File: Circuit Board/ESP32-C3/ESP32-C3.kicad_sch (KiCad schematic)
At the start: 19 parts

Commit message: Exposed General Purpose SPI & LED
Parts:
- added R?: 22R, symbol Device:R
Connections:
- net INT_ACC: now reaches U?.10 (MTDI/GPIO5/ADC2_CH0)
- net FSPI_CLK: now reaches U?.12 (MTCK/GPIO6)
- net FSPI_CLK: now also R?.2
- net FSPI_D: now reaches U?.13 (MTDO/GPIO7)
- net LED B: now reaches U?.9 (MTMS/GPIO4/ADC1_CH4)
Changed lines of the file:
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@@
     (stroke (width 0) (type default) (color 0 0 0 0))
   )
-  (wire (pts (xy 106.553 93.98) (xy 114.935 93.98))
+  (wire (pts (xy 94.996 93.98) (xy 114.935 93.98))
     (stroke (width 0) (type default) (color 0 0 0 0))
   )
@@
     (stroke (width 0) (type default) (color 0 0 0 0))
   )
+  (wire (pts (xy 104.648 99.06) (xy 114.935 99.06))
+    (stroke (width 0) (type default) (color 0 0 0 0))
+  )
   (wire (pts (xy 192.786 114.935) (xy 190.754 114.935))
     (stroke (width 0) (type default) (color 0 0 0 0))
@@
     (stroke (width 0) (type default) (color 0 0 0 0))
   )
-  (wire (pts (xy 106.553 96.52) (xy 114.935 96.52))
+  (wire (pts (xy 94.996 96.52) (xy 114.935 96.52))
     (stroke (width 0) (type default) (color 0 0 0 0))
   )
@@
     (stroke (width 0) (type default) (color 0 0 0 0))
   )
-  (wire (pts (xy 106.68 101.6) (xy 114.935 101.6))
+  (wire (pts (xy 94.996 101.6) (xy 114.935 101.6))
     (stroke (width 0) (type default) (color 0 0 0 0))
   )
@@
     (stroke (width 0) (type default) (color 0 0 0 0))
   )
-  (wire (pts (xy 106.553 99.06) (xy 114.935 99.06))
+  (wire (pts (xy 94.996 99.06) (xy 97.028 99.06))
     (stroke (width 0) (type default) (color 0 0 0 0))
   )
@@
   (text "CL=2*(CLO-Cs)=2*(10-5)pF=10pF" (at 72.136 53.594 0)
     (effects (font (size 1 1)) (justify left bottom))
+  )
+  (label "LED B" (at 106.299 93.98 0)
+    (effects (font (size 1.27 1.27)) (justify left bottom))
+  )
+  (label "FSPI_D" (at 105.029 101.6 0)
+    (effects (font (size 1.27 1.27)) (justify left bottom))
+  )
+  (label "FSPI_CLK" (at 105.029 99.06 0)
+    (effects (font (size 1.27 1.27)) (justify left bottom))
+  )
+  (label "INT_ACC" (at 105.41 96.52 0)
+    (effects (font (size 1.27 1.27)) (justify left bottom))
   )
   (global_label "SPI_NCS" (shape input) (at 171.958 96.52 0) (fields_autoplaced)
@@
     (pin "2")
   )
+  (symbol (lib_id "Device:R") (at 100.838 99.06 90) (unit 1)
+    (in_bom yes) (on_board yes)
+    (property "Reference" "R?" (id 0) (at 97.028 97.536 90))
+    (property "Value" "22R" (id 1) (at 100.711 99.187 90))
+    (property "Footprint" "" (id 2) (at 100.838 100.838 90)
+      (effects (font (size 1.27 1.27)) hide)
+    )
+    (property "Datasheet" "~" (id 3) (at 100.838 99.06 0)
+      (effects (font (size 1.27 1.27)) hide)
+    )
+    (pin "1")
+    (pin "2")
+  )
   (symbol (lib_id "Device:C") (at 118.364 56.642 0) (unit 1)
     (in_bom yes) (on_board yes) (fields_autoplaced)
@@
       (reference "R?") (unit 1) (value "22R") (footprint "")
     )
+    (path "/87b79b9a-bd1e-435d-9300-858b5850ef25"
+      (reference "R?") (unit 1) (value "22R") (footprint "")
+    )

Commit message: Added UART Pinout
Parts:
- added R? (x2): 470R, symbol Device:R
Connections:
- net at U?.27 (U0RXD/GPIO20): now also R?.1
- net at U?.28 (U0TXD/GPIO21): now also R?.1
- new net UART0_RX: R?.2
- new net UART0_TX: R?.2
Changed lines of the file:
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@@
+    (stroke (width 0) (type default) (color 0 0 0 0))
+  )
+  (wire (pts (xy 186.309 73.66) (xy 191.77 73.66))
     (stroke (width 0) (type default) (color 0 0 0 0))
   )
@@
     (stroke (width 0) (type default) (color 0 0 0 0))
   )
+  (wire (pts (xy 186.309 71.12) (xy 191.77 71.12))
+    (stroke (width 0) (type default) (color 0 0 0 0))
+  )
   (wire (pts (xy 112.268 51.054) (xy 118.364 51.054))
     (stroke (width 0) (type default) (color 0 0 0 0))
@@
     (stroke (width 0) (type default) (color 0 0 0 0))
   )
+  (wire (pts (xy 170.815 71.12) (xy 178.689 71.12))
+    (stroke (width 0) (type default) (color 0 0 0 0))
+  )
   (wire (pts (xy 78.105 124.46) (xy 66.675 124.46))
     (stroke (width 0) (type default) (color 0 0 0 0))
@@
   )
   (wire (pts (xy 175.895 124.46) (xy 175.895 128.27))
+    (stroke (width 0) (type default) (color 0 0 0 0))
+  )
+  (wire (pts (xy 170.815 73.66) (xy 178.689 73.66))
     (stroke (width 0) (type default) (color 0 0 0 0))
   )
@@
     (effects (font (size 1.27 1.27)) (justify left bottom))
   )
+  (label "UART0_RX" (at 187.071 73.66 0)
+    (effects (font (size 1.27 1.27)) (justify left bottom))
+  )
   (label "FSPI_D" (at 105.029 101.6 0)
     (effects (font (size 1.27 1.27)) (justify left bottom))
@@
   )
   (label "INT_ACC" (at 105.41 96.52 0)
+    (effects (font (size 1.27 1.27)) (justify left bottom))
+  )
+  (label "UART0_TX" (at 187.198 71.12 0)
     (effects (font (size 1.27 1.27)) (justify left bottom))
   )
@@
     (pin "2")
   )
+  (symbol (lib_id "Device:R") (at 182.499 73.66 90) (unit 1)
+    (in_bom yes) (on_board yes)
+    (property "Reference" "R?" (id 0) (at 182.499 75.692 90))
+    (property "Value" "470R" (id 1) (at 182.499 73.787 90))
+    (property "Footprint" "" (id 2) (at 182.499 75.438 90)
+      (effects (font (size 1.27 1.27)) hide)
+    )
+    (property "Datasheet" "~" (id 3) (at 182.499 73.66 0)
+      (effects (font (size 1.27 1.27)) hide)
+    )
+    (pin "1")
+    (pin "2")
+  )
   (symbol (lib_id "power:GND") (at 121.92 147.955 0) (unit 1)
     (in_bom yes) (on_board yes) (fields_autoplaced)
@@
     )
     (property "Datasheet" "~" (id 3) (at 131.445 135.89 0)
+      (effects (font (size 1.27 1.27)) hide)
+    )
+    (pin "1")
+    (pin "2")
+  )
+  (symbol (lib_id "Device:R") (at 182.499 71.12 90) (unit 1)
+    (in_bom yes) (on_board yes)
+    (property "Reference" "R?" (id 0) (at 182.499 69.215 90))
+    (property "Value" "470R" (id 1) (at 182.499 71.247 90))
+    (property "Footprint" "" (id 2) (at 182.499 72.898 90)
+      (effects (font (size 1.27 1.27)) hide)
+    )
+    (property "Datasheet" "~" (id 3) (at 182.499 71.12 0)
       (effects (font (size 1.27 1.27)) hide)
     )
@@
       (reference "R?") (unit 1) (value "22R") (footprint "")
     )
+    (path "/4c20fbfb-2772-4ac7-943c-c67b70ee00e3"
+      (reference "R?") (unit 1) (value "470R") (footprint "")
+    )
     (path "/87b79b9a-bd1e-435d-9300-858b5850ef25"
       (reference "R?") (unit 1) (value "22R") (footprint "")
@@
       (reference "R?") (unit 1) (value "5k1") (footprint "")
     )
+    (path "/d053cebc-ddcc-4fe9-8757-cc44e8daedcd"
+      (reference "R?") (unit 1) (value "470R") (footprint "")
+    )
     (path "/fe4df71a-c9dd-4482-86ce-3213aba20d79"

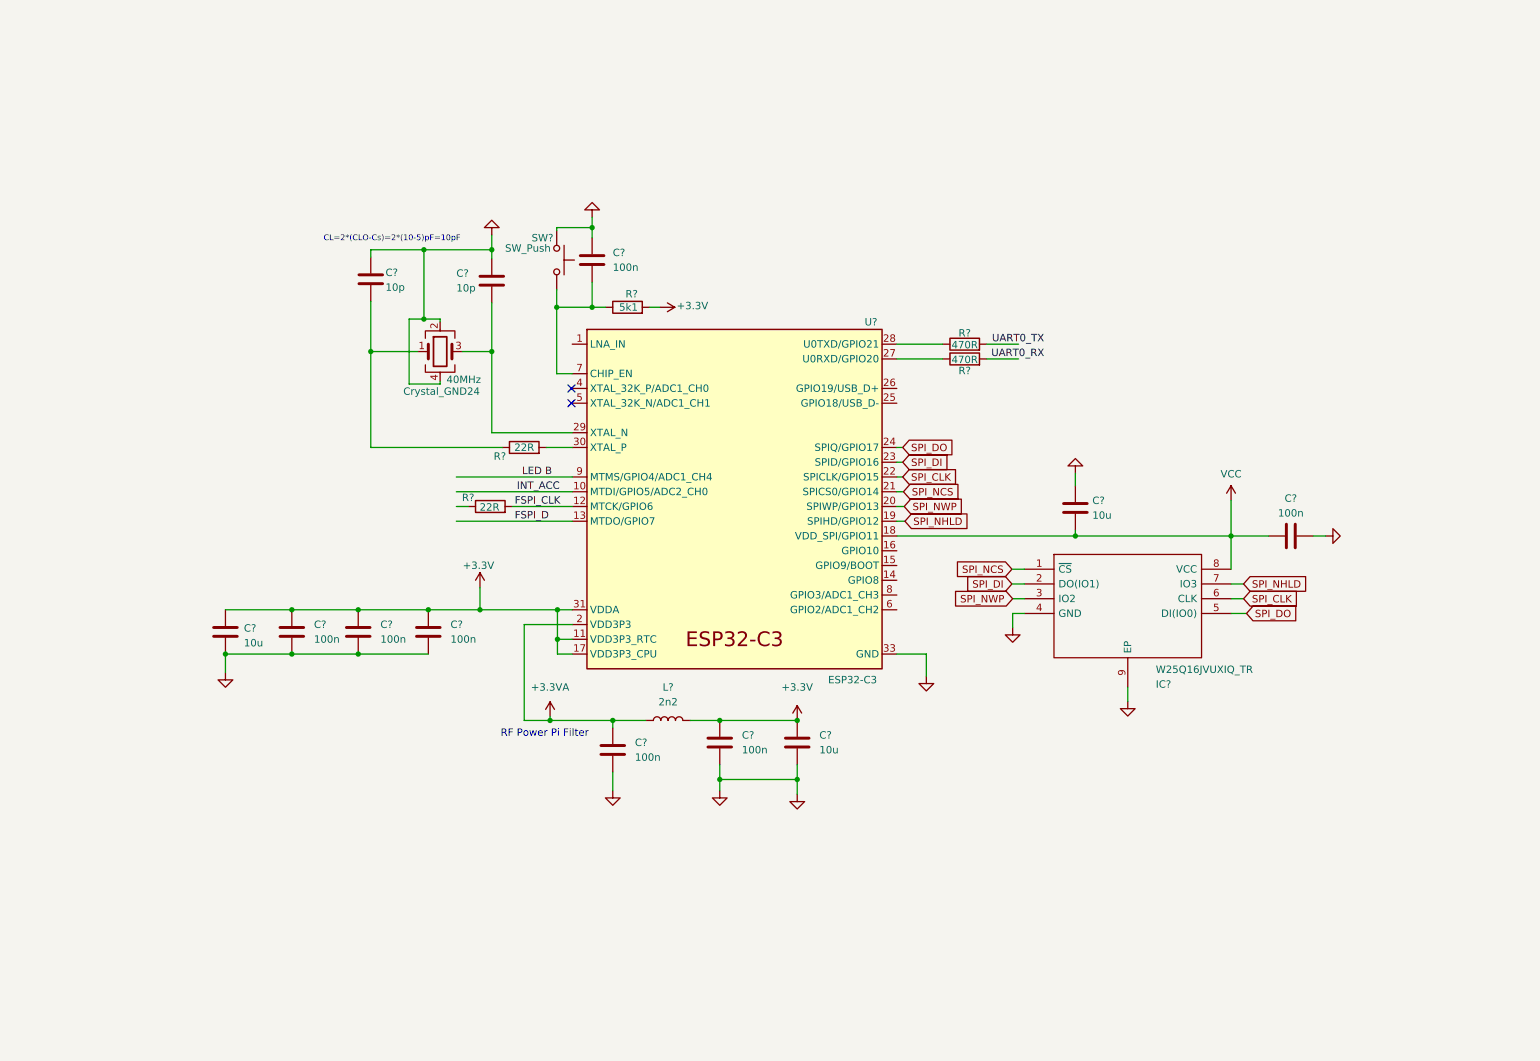
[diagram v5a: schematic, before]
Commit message: Added power regulator for USB C connector
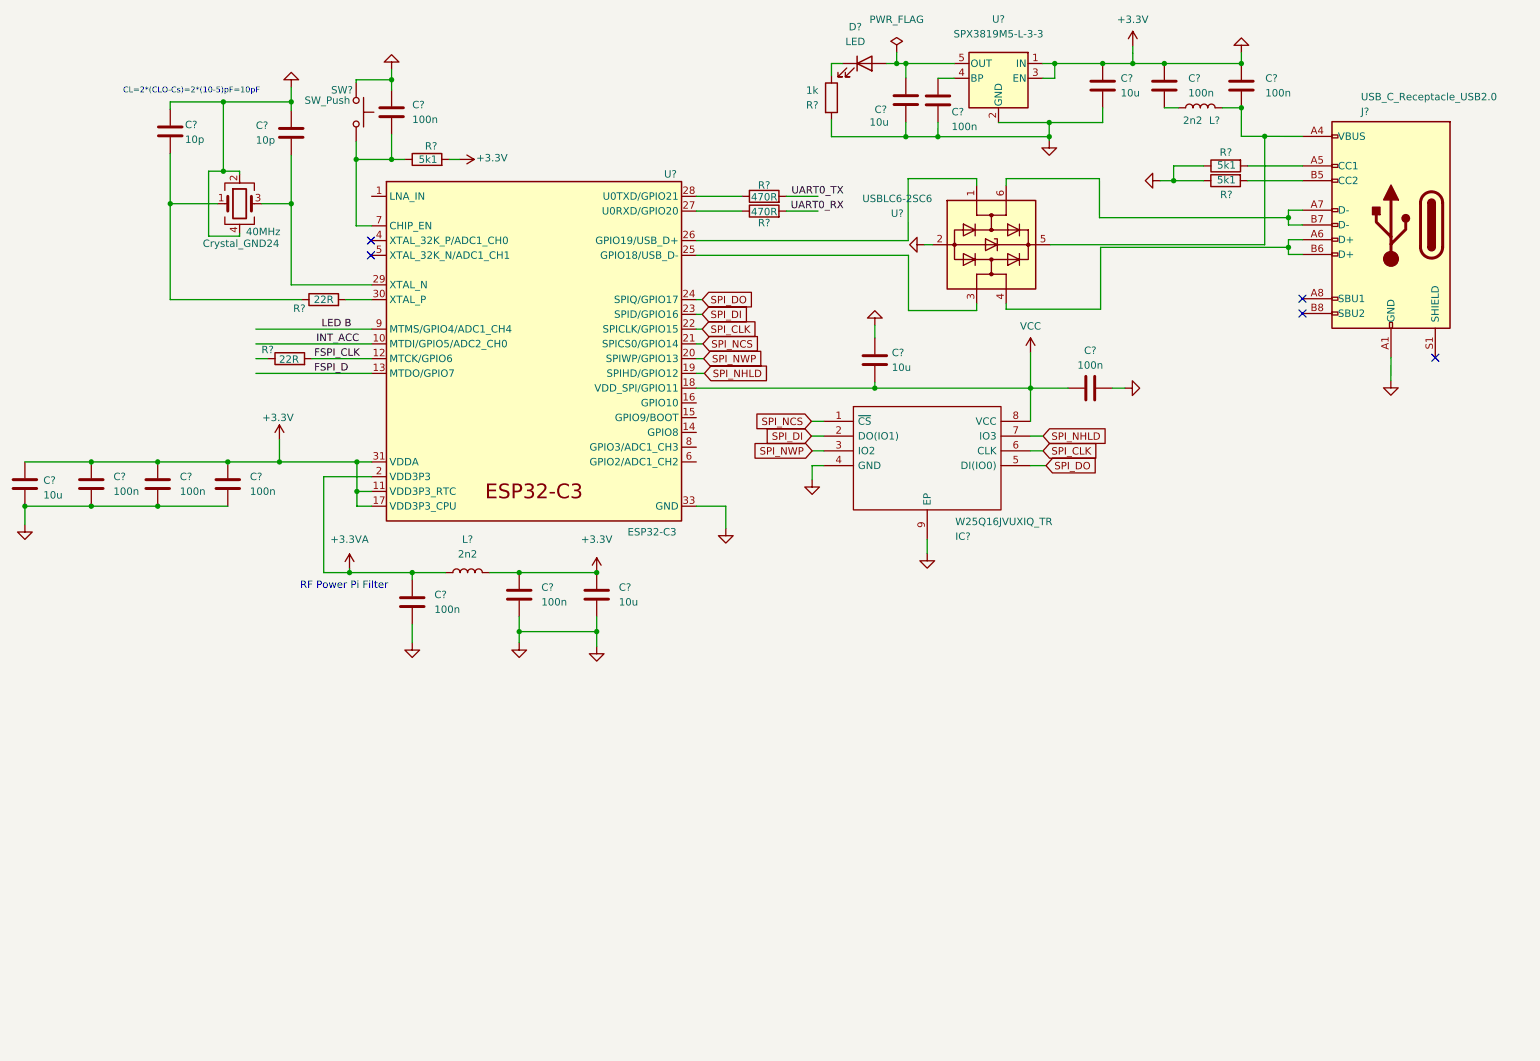
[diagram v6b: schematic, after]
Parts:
- added C? (x3): 100n, symbol Device:C
- added C? (x2): 10u, symbol Device:C
- added D?: LED, symbol Device:LED
- added J?: USB_C_Receptacle_USB2.0, symbol Connector:USB_C_Receptacle_USB2.0
- added L?: 2n2, symbol Device:L
- added R? (x2): 5k1, symbol Device:R
- added R?: 1k, symbol Device:R
- added U?: USBLC6-2SC6, Package_TO_SOT_SMD:SOT-23-6, symbol Power_Protection:USBLC6-2SC6
- added U?: SPX3819M5-L-3-3, Package_TO_SOT_SMD:SOT-23-5, symbol Regulator_Linear:SPX3819M5-L-3-3
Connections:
- net GND is gone; now on net +3.3V: 40MHz.2, 40MHz.4, C?.1, C?.1, C?.1, C?.1, C?.2, C?.2, C?.2, C?.2, C?.2, C?.2, C?.2, C?.2, IC?.4 (GND), IC?.9 (EP), SW?.1, U?.33 (GND)
- net +3.3V: now also C?.1, C?.1, C?.1, C?.2, C?.2, C?.2, J?.A1 (GND), J?.A12 (GND), J?.B1 (GND), J?.B12 (GND), R?.1, R?.1, R?.2, U?.1 (IN), U?.2 (GND), U?.2 (GND), U?.3 (EN)
- net at U?.25 (GPIO18/USB_D-): now also U?.3 (I/O2)
- net at U?.26 (GPIO19/USB_D+): now also U?.1 (I/O1)
- new net: J?.A6 (D+), J?.B6 (D+), U?.4 (I/O2)
- new net: C?.2, J?.A4 (VBUS), J?.A9 (VBUS), J?.B4 (VBUS), J?.B9 (VBUS), L?.2, U?.5 (VBUS)
- new net: J?.A7 (D-), J?.B7 (D-), U?.6 (I/O1)
- new net: C?.1, U?.4 (BP)
- new net: C?.1, D?.2 (A), U?.5 (OUT)
- new net: C?.2, L?.1
- new net: J?.B5 (CC2), R?.2
- new net: J?.A5 (CC1), R?.2
- new net: D?.1 (K), R?.1
- no-connect marks 2 -> 5
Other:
- moved on the sheet: 40MHz, C?, IC?, L?, R?, SW?, U?

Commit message: Added Auxiliary UART Pins
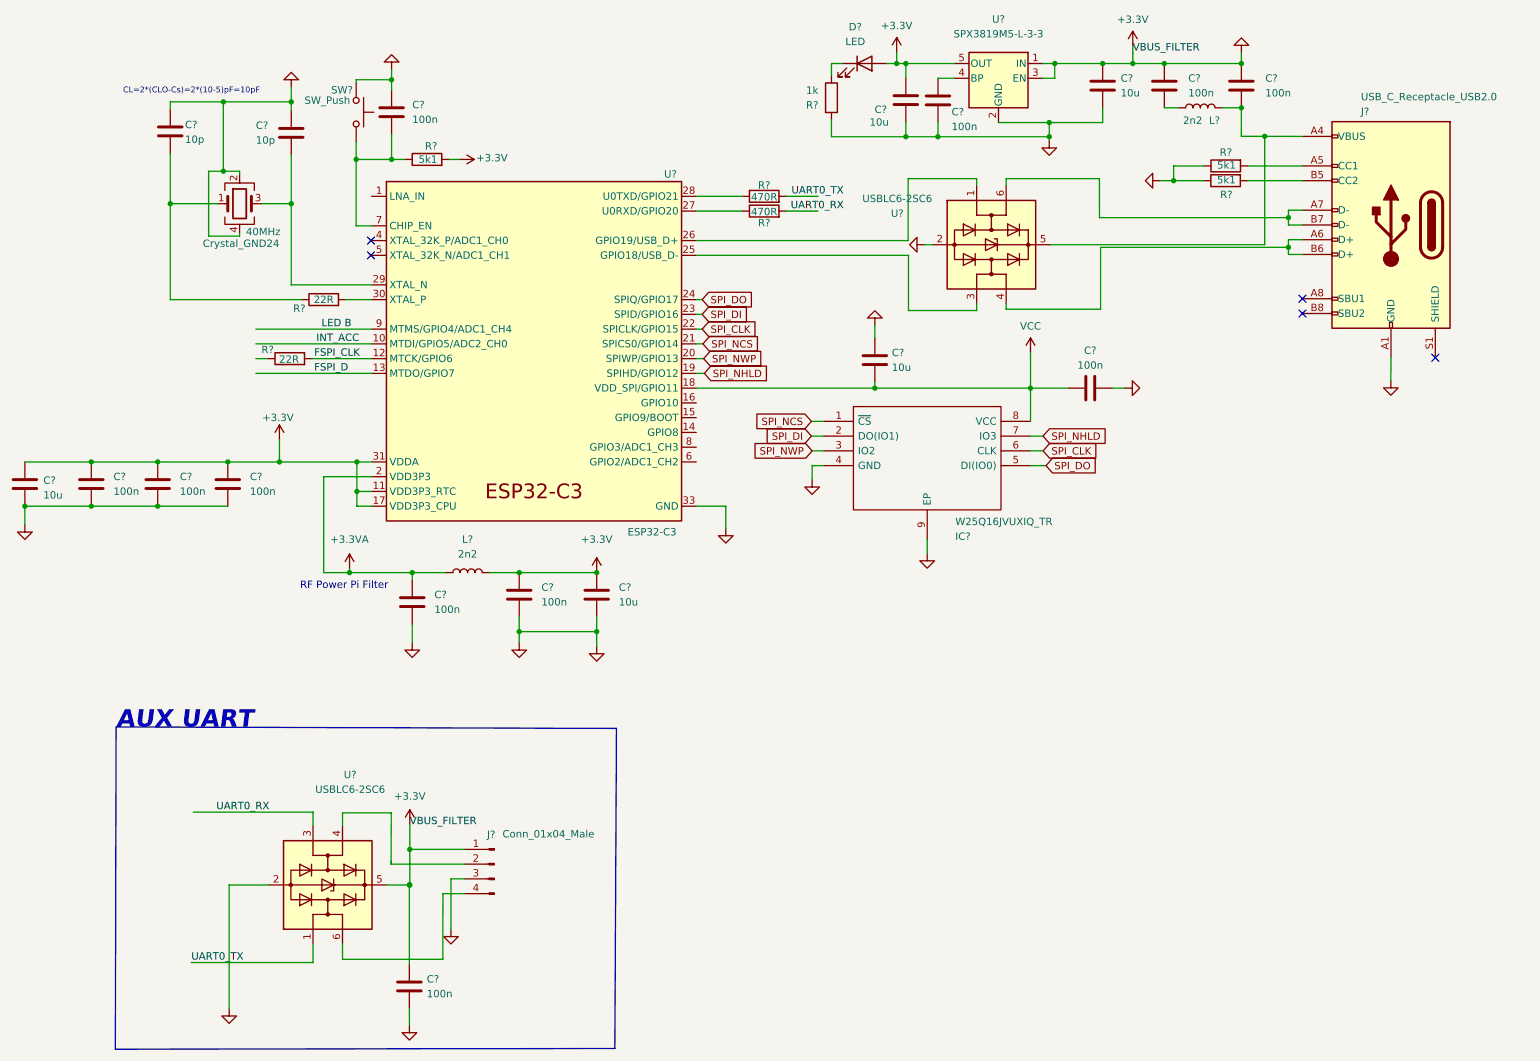
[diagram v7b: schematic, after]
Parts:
- added C?: 100n, symbol Device:C
- added J?: Conn_01x04_Male, Connector_PinHeader_2.00mm:PinHeader_1x04_P2.00mm_Vertical, symbol Connector:Conn_01x04_Male
- added U?: USBLC6-2SC6, Package_TO_SOT_SMD:SOT-23-6, symbol Power_Protection:USBLC6-2SC6
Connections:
- net +3.3V: now also C?.1, D?.2 (A), U?.5 (OUT), C?.1, C?.2, J?.1 (Pin_1), J?.3 (Pin_3), U?.2 (GND), U?.5 (VBUS)
- net UART0_RX: now also U?.3 (I/O2)
- net UART0_TX: now also U?.1 (I/O1)
- new net: J?.2 (Pin_2), U?.4 (I/O2)
- new net: J?.4 (Pin_4), U?.6 (I/O1)
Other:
- note added: "AUX UART"
